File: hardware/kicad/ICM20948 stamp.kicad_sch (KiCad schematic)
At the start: 11 parts, among them U101 ICM-20948, U102 TXS0108EPW

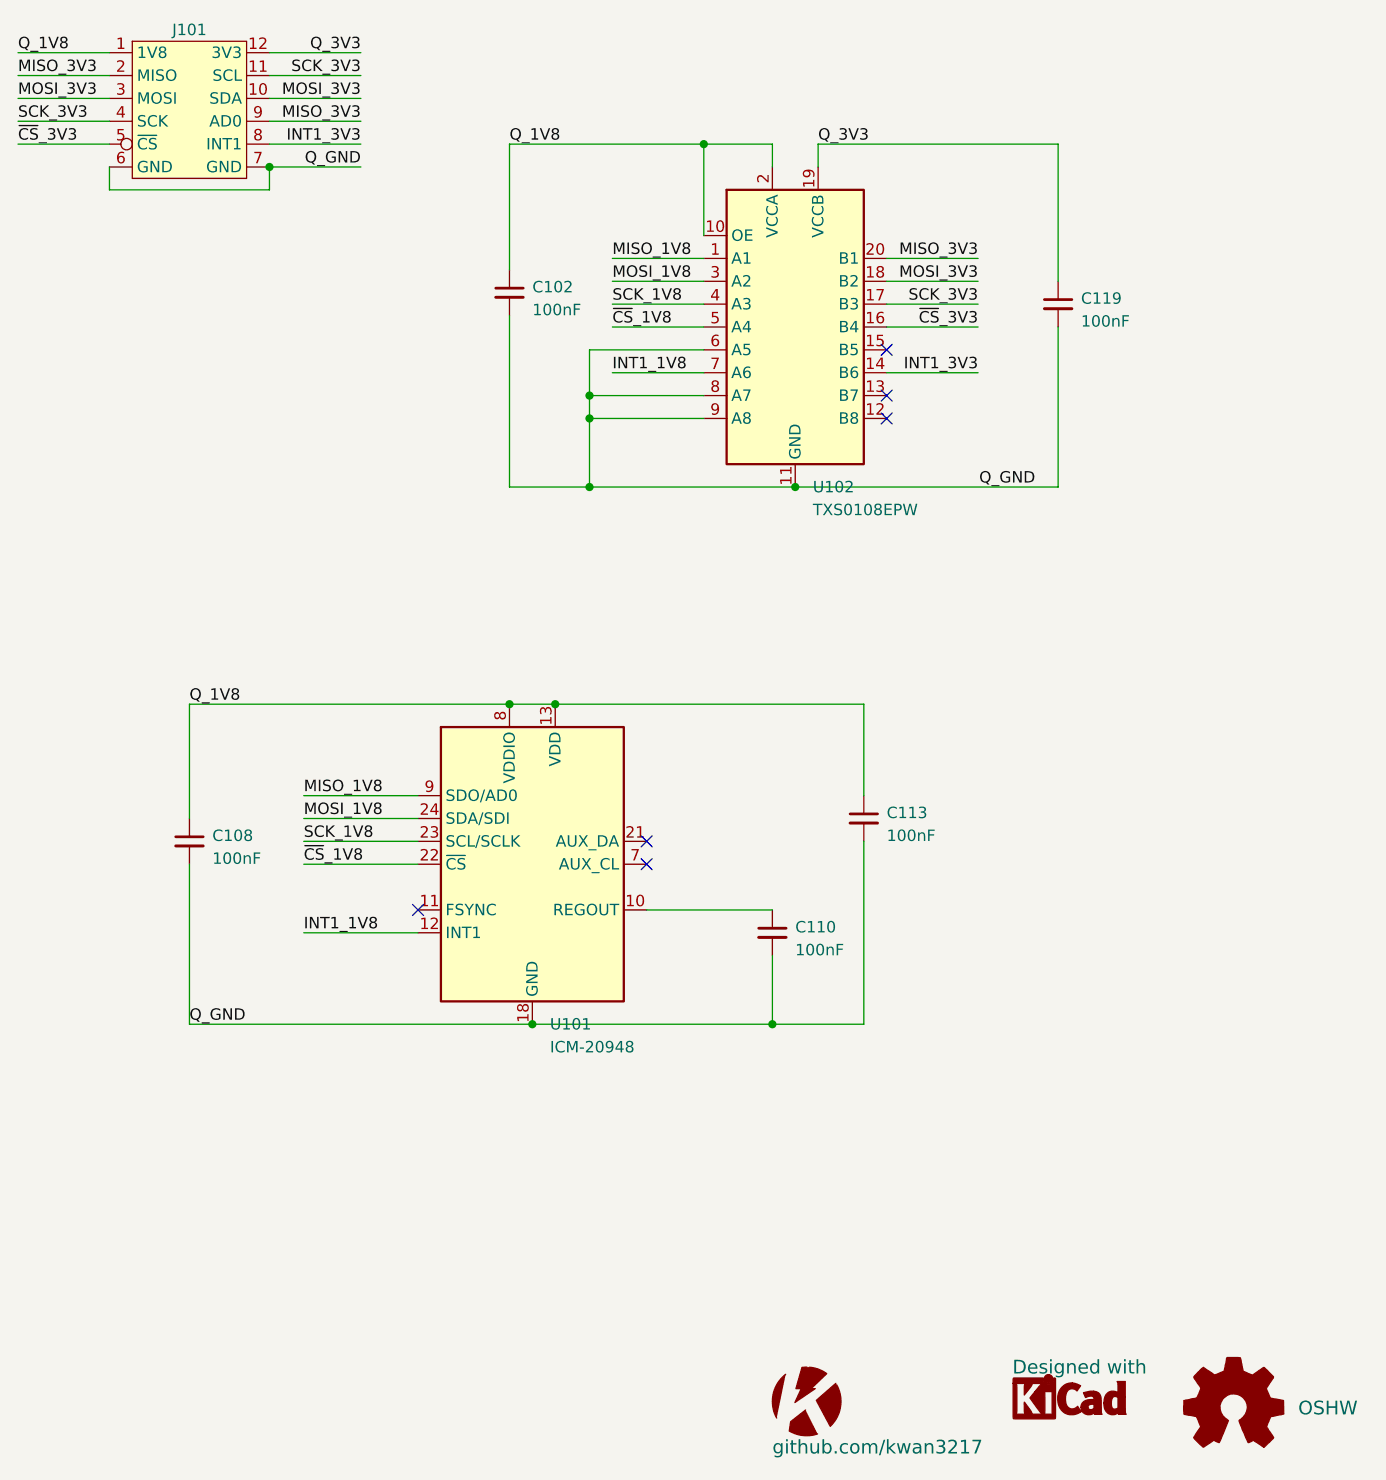
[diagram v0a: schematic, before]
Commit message: Imported shipometer hat 23.04 as built, updated to Kicad 9
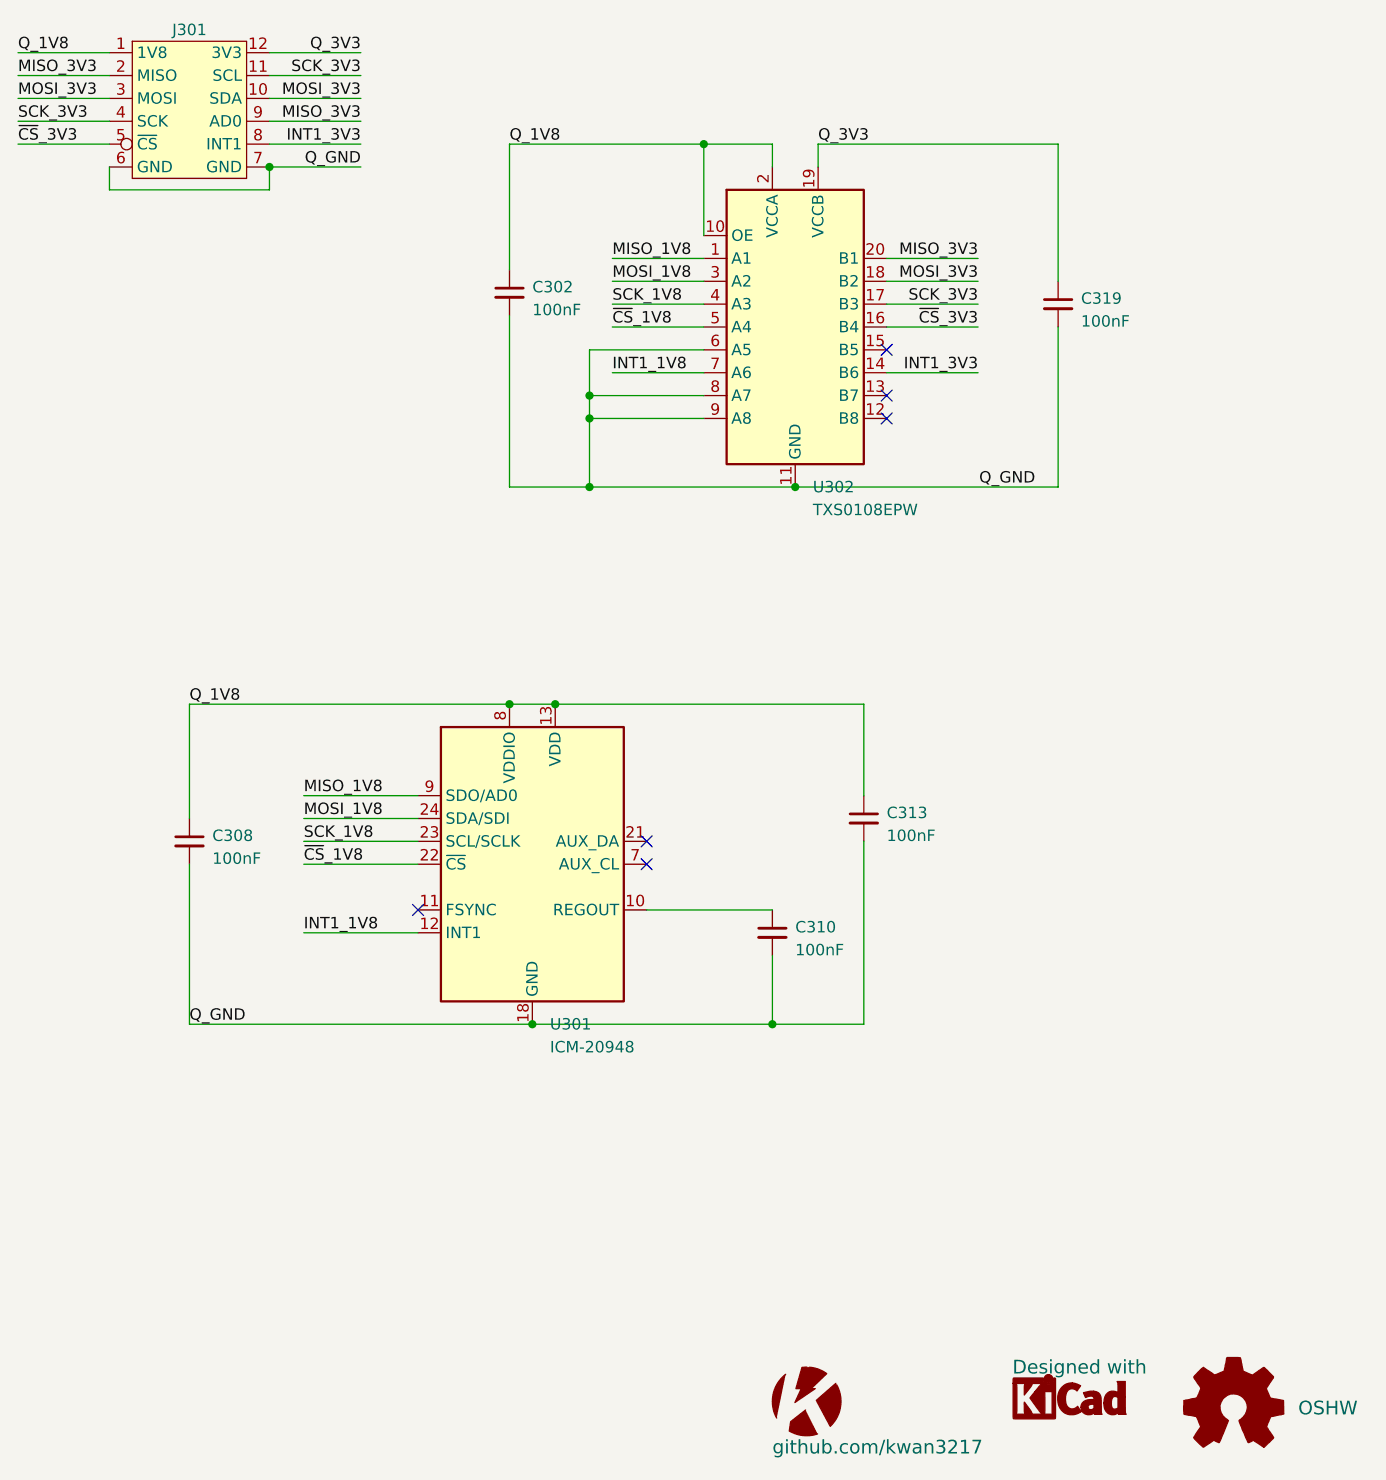
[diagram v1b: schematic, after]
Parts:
- renumbered C102 to C302, C108 to C308, C110 to C310, C113 to C313, C119 to C319, G1 to G301, G2 to G302, G3 to G303, J101 to J301, U101 to U301, U102 to U302
